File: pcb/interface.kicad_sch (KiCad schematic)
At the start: 10 parts, among them J1 AVR-UPDI-6, J2 QWICC, J3 Power In, J4 Power Out

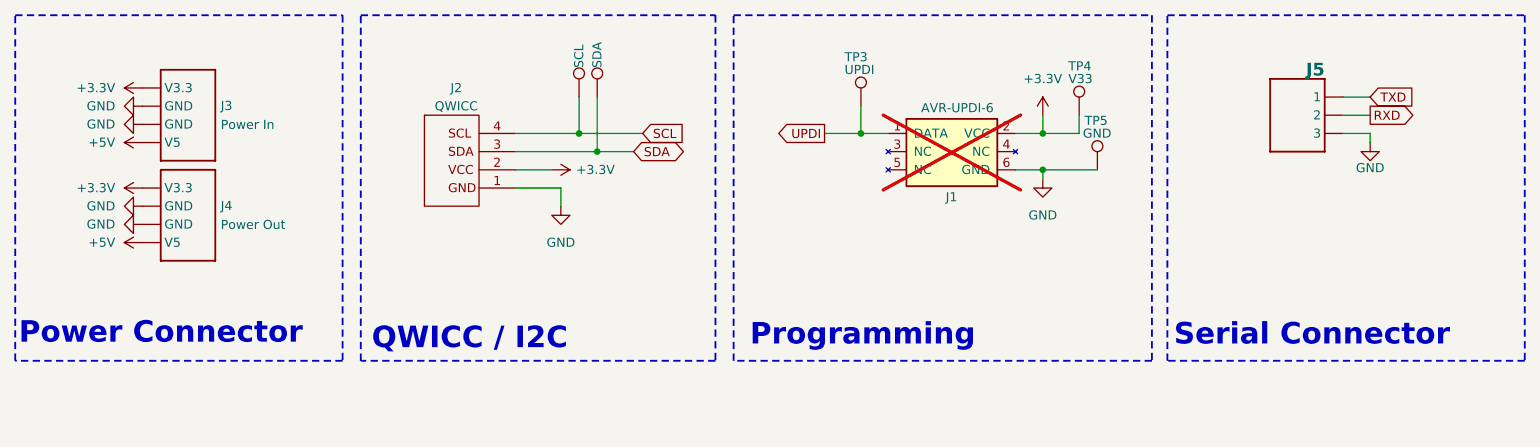
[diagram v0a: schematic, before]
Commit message: Updated to latest libraries
Changed to all CRG footprints (mostly)
Moved somethings around
Added LED jumper
Updated symbols/logos
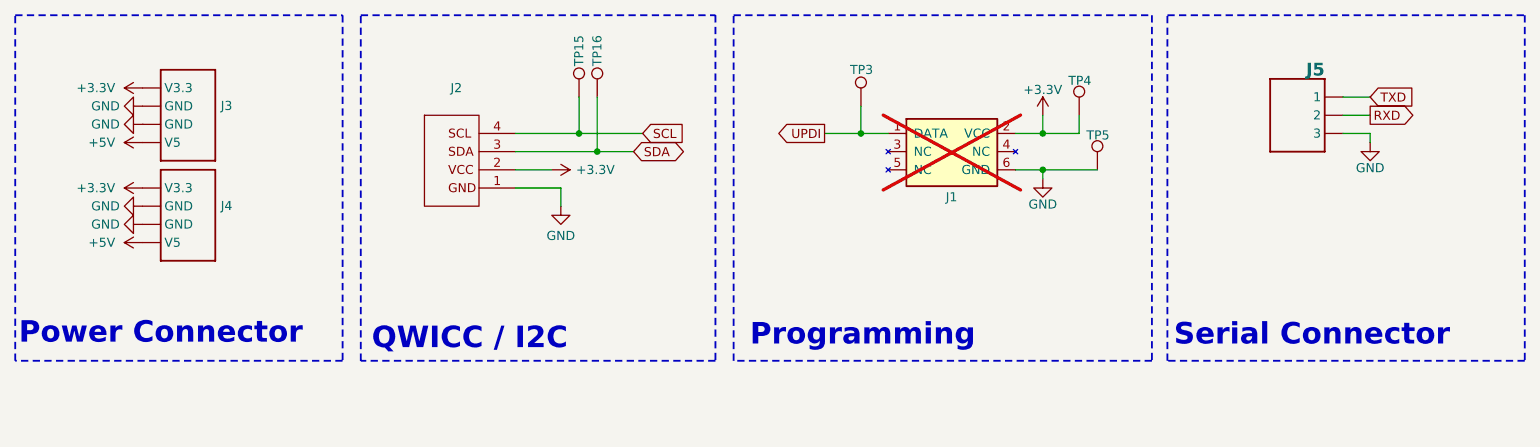
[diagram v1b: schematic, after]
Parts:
- J2: value QWICC -> ~; Mouser 306-SM04BSRSSTBTLFSN -> 306-SM04B-SRSS-TBTLFSN
- J3: value Power In -> ~
- J4: value Power Out -> ~
- J5: footprint Connector_JST:JST_SH_BM03B-SRSS-TB_1x03-1MP_P1.00mm_Vertical -> CRGM Connector:JST_SH_BM03B-SRSS-TB_1x03-1MP_P1.00mm_Vertical; Digikey (none) -> 455-BM04B-SRSS-TBTR-ND; LCSC C2919600 -> C2919601; MPN BM03B-SRSS-TB -> BM04B-SRSS-TB; Mouser (none) -> 306-BM04BSRSSTBTLFSN
- TP15: value SCL -> ~; symbol Connector:TestPoint -> CRGM Connector:TestPoint
- TP16: value SDA -> ~; symbol Connector:TestPoint -> CRGM Connector:TestPoint
- TP3: value UPDI -> ~; symbol Connector:TestPoint -> CRGM Connector:TestPoint
- TP4: value V33 -> ~; symbol Connector:TestPoint -> CRGM Connector:TestPoint
- TP5: value GND -> ~; symbol Connector:TestPoint -> CRGM Connector:TestPoint

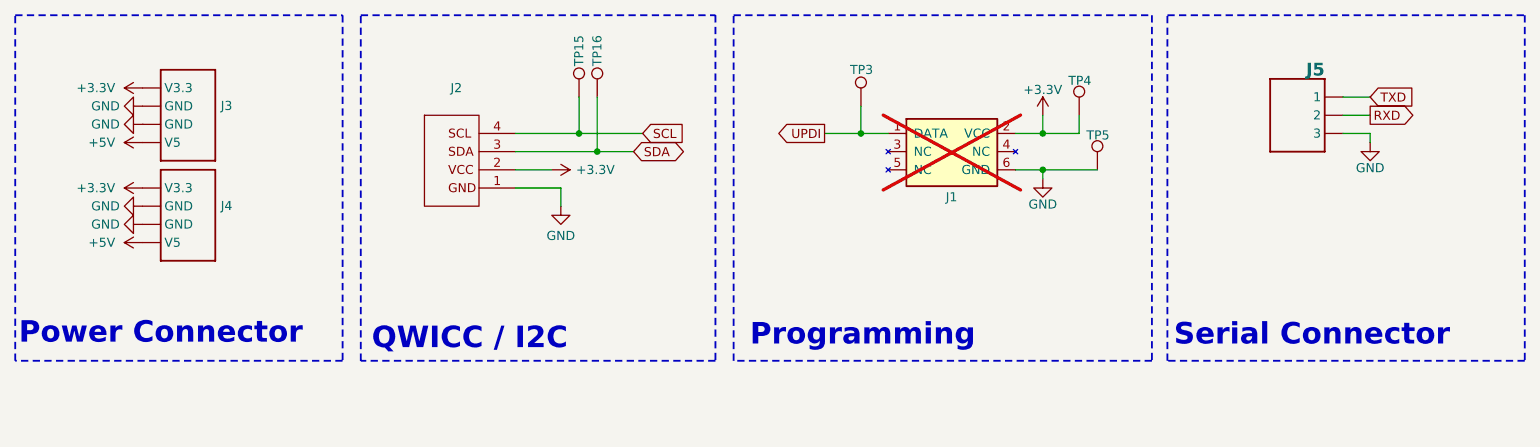
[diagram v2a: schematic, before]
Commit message: Updated for consistency
Updated footprints
Added ESD to power
Added second QWICC connector
Rerouted as required
Made mounting holes grounded
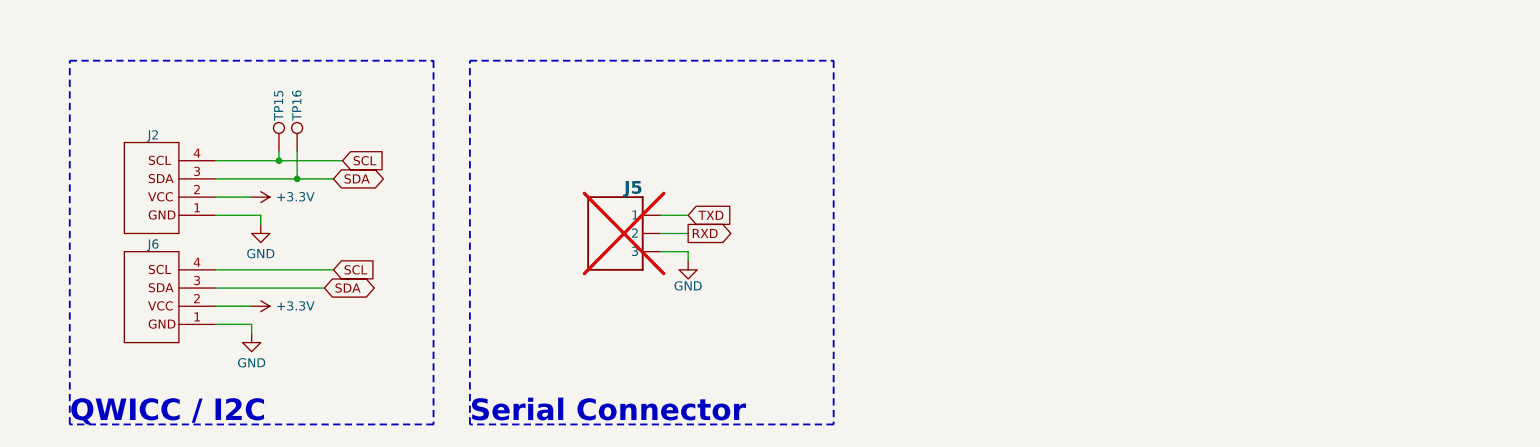
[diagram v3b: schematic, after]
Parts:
- removed J1: AVR-UPDI-6, CRGM Connector:PinHeader_2x03_P2.54mm_Vertical_SMD, symbol CRGM Connector:AVR-UPDI-6
- removed J3, J4: ~, CRGM Connector:JST_SH_SM04B-SRSS-TB_1x04-1MP_P1.00mm_Horizontal, symbol CRGM Connector:AQ_POWER
- removed TP3, TP4, TP5: ~, CRGM Mechanical:TestPoint_Pad_D1.0mm, symbol CRGM Connector:TestPoint
- added J6: ~, CRGM Connector:JST_SH_SM04B-SRSS-TB_1x04-1MP_P1.00mm_Horizontal, symbol CRGM Connector:QWIIC
- J2: Mouser 306-SM04B-SRSS-TBTLFSN -> 306-SM04BSRSSTBTLFSN
- J5: now not fitted; now left out of the parts list
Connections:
- net +3.3V: now also J6.2
- net GND: now also J6.1
- net SCL: now also J6.4
- net SDA: now also J6.3
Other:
- note removed: "Power Connector"
- note removed: "Programming"
- moved on the sheet: J2, TP15, TP16

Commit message: Updated I2C pulls to open jumper
Fixed I2C to be open rather than bridged.
Changed opto-isolator to CRGM library.
Updated picture of bottom side to match new footprint
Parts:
- TP15, TP16: now left out of the parts list
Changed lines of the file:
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@@
+			)
+		)
+		(property "Sim.Enable" ""
+			(at 33.02 36.83 0)
+			(effects
+				(font
+					(size 1.27 1.27)
+				)
+				(hide yes)
 			)
 		)
@@
 			)
 		)
+		(property "Sim.Enable" ""
+			(at 105.41 46.99 0)
+			(effects
+				(font
+					(size 1.27 1.27)
+				)
+				(hide yes)
+			)
+		)
 		(pin "1"
 		)
@@
 		(unit 1)
 		(exclude_from_sim no)
-		(in_bom yes)
+		(in_bom no)
 		(on_board yes)
 		(dnp no)
@@
 		(property "Description" "Test Point D1.0mm"
 			(at 54.61 47.244 0)
+			(effects
+				(font
+					(size 1.27 1.27)
+				)
+				(hide yes)
+			)
+		)
+		(property "Sim.Enable" ""
+			(at 54.61 38.1 90)
 			(effects
 				(font
@@
 		(unit 1)
 		(exclude_from_sim no)
-		(in_bom yes)
+		(in_bom no)
 		(on_board yes)
 		(dnp no)
@@
 		(property "Description" "Test Point D1.0mm"
 			(at 57.15 47.244 0)
+			(effects
+				(font
+					(size 1.27 1.27)
+				)
+				(hide yes)
+			)
+		)
+		(property "Sim.Enable" ""
+			(at 57.15 38.1 90)
 			(effects
 				(font
@@
 			(at 33.02 52.07 0)
 			(effects
+				(font
+					(size 1.27 1.27)
+				)
+				(hide yes)
+			)
+		)
+		(property "Sim.Enable" ""
+			(at 33.02 52.07 0)
+			(effects

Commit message: Updated for consistency with new patterns
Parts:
- removed J5: ~, CRGM Connector:JST_SH_BM03B-SRSS-TB_1x03-1MP_P1.00mm_Vertical, symbol CRGM Connector:JST-SH-3
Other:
- note removed: "Serial Connector"
